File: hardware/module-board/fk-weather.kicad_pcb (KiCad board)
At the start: 2 copper layers, 37.5 x 103 mm, 72 parts, among them J1 MICRO-USB, J10 Conn_01x06, J11 Conn_01x06, J2 Conn_01x05, J3 CONN_01x03_SERIAL, J4 Conn_01x04, J5 Conn_01x02, J6 CONN_02x05_SWD, J7 Conn_01x05, Q4 2N7002LT1G, SW1 SPNO, U1 ATSAMD21G18A-AU, U2 MCP1700T-XXX2E, U3 TPS2051B, U4 S25FL1xxK0XM, U5 SK6812, U6 PCF8523, Y1 FC-135, Y2 FC-135

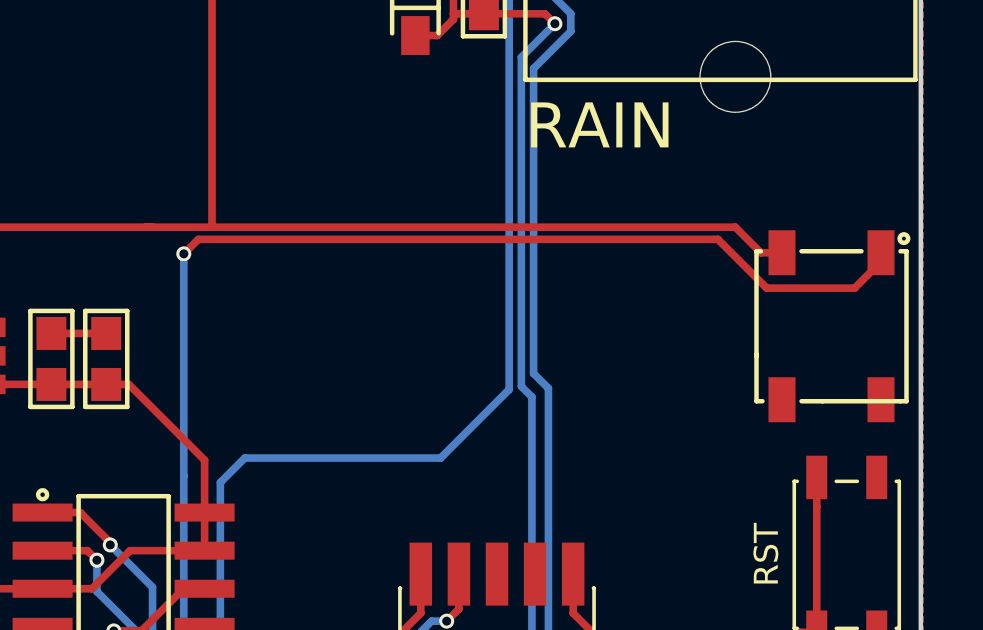
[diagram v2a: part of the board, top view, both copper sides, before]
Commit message: Fix SK6812 and cleanup signal naming.
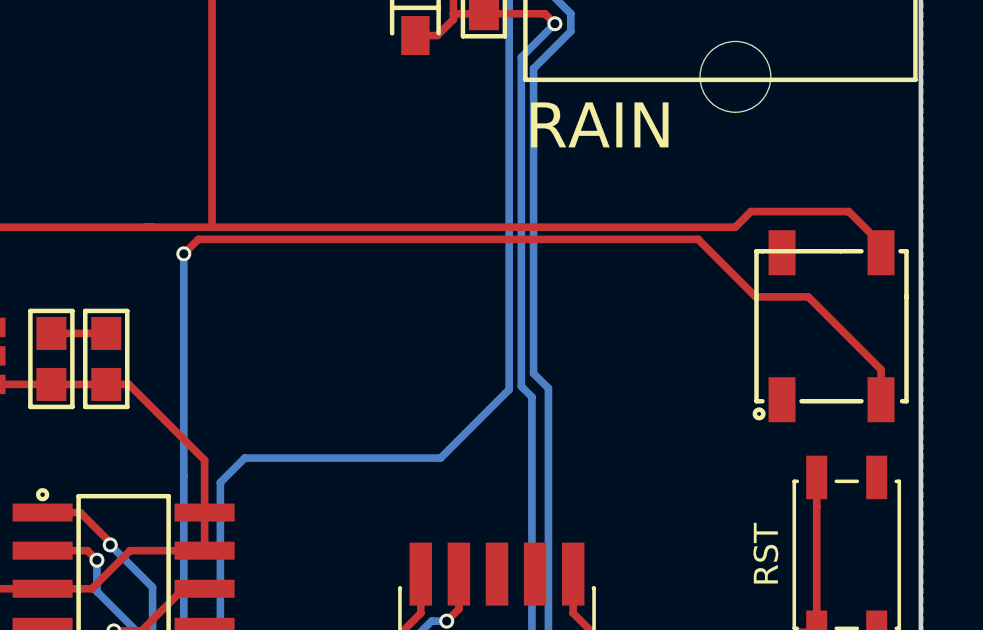
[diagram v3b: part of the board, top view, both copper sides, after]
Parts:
- C14: value 4.7uF 10V X5R -> 4.7uF
- C5: value 1uF 10V X5R -> 1uF
- J4: value Conn_01x04 -> CONN_01x04
- R8: value 100k -> 100K
- U2: value MCP1700T-XXX2E -> MCP1700T-3302E/MB
- U4: value S25FL1xxK0XM -> S25FL116K0XMFI041
- turned U5 to 270 degrees
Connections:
- net /FLASH_CS renamed /D5_FLASH_CS
- net /PERIPH_EN renamed /D8_PERIPH_EN
- net /RAIN renamed /D6_RAIN
- net /WIND_DIR renamed /A1_WIND_DIR
- net /WIND_SPEED renamed /D10_WIND_SPEED
- U5 pad 1: /A3 -> GND
- U5 pad 2: 3V3 -> /A3
- U5 pad 3: Net-(U5-Pad3) -> 3V3
- U5 pad 4: GND -> Net-(U5-Pad4)
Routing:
- net 3V3: track 285.5 -> 289.4 mm
- net /A3: track 52.1 -> 53.2 mm

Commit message: Fix rescued stuff and clear DRC problems.
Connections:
- net AREF renamed Net-(C14-Pad1)

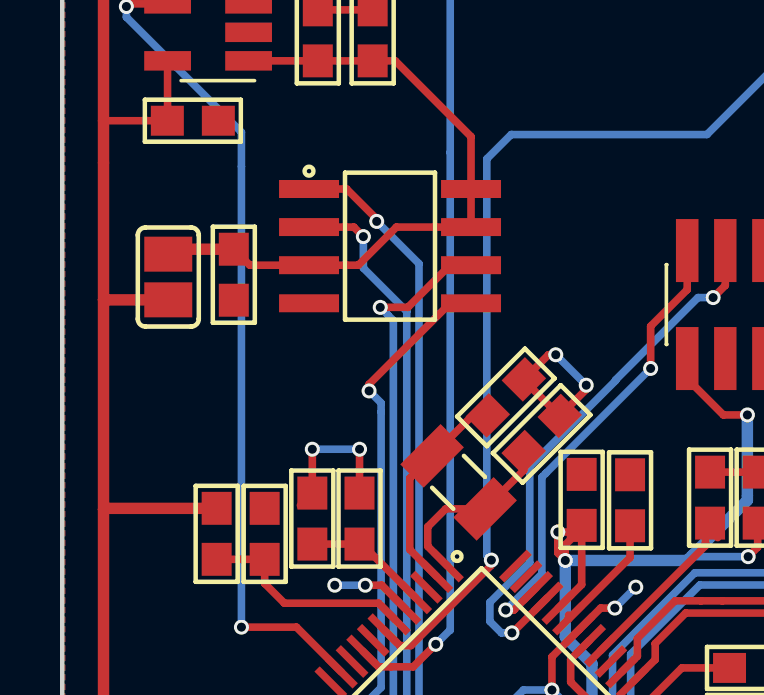
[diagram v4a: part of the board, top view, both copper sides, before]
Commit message: Use more compatible FP for flash.
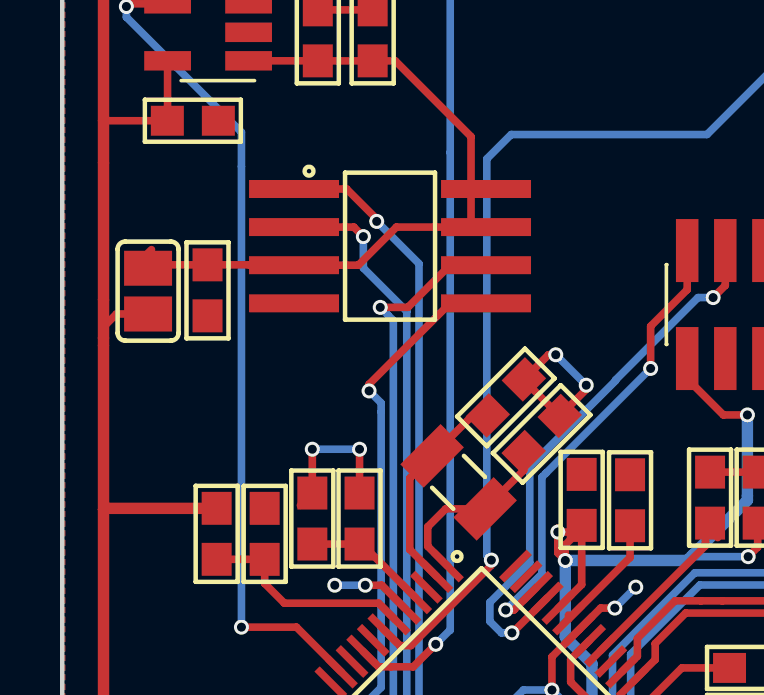
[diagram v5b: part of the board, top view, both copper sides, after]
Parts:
- U4: footprint conservify:SOIC-8-N -> conservify:SOIC-8-N-WIDE
- moved C18 1.02 mm to (89.4, 149.0)
- moved J5 0.82 mm to (87.5, 149.1)
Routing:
- net /PERIPH_3V3: track 22.4 -> 24.3 mm
- net 3V3: track 289.4 -> 290.4 mm

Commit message: Schematic/FP cleanup. Nothing major.
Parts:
- J10, J11: value Conn_01x06 -> CONN_01x06; footprint conservify:wurth_615006138421 -> conservify:WURTH_615006138421
- J2, J7: value Conn_01x05 -> CONN_01x05
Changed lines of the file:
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@@
       (xy -6.476371 -1.79874)) (layer F.SilkS) (width 0.01))
-  )
-  (module conservify:wurth_615006138421 (layer F.Cu)
-    (at 115.923028 125.132668 270)
-    (fp_text reference J10 (at 0 -3.01244 270) (layer F.SilkS) hide
-      (effects (font (size 0.762 0.762) (thickness 0.15)))
-    )
-    (fp_text value Conn_01x06 (at 0 0 270) (layer F.SilkS) hide
-      (effects (font (size 0.508 0.508) (thickness 0.127)))
-    )
-    (fp_line (start -6.1 -6) (end -6.1 7) (layer F.SilkS) (width 0.15))
-    (fp_line (start -6.1 7) (end 6.1 7) (layer F.SilkS) (width 0.15))
-    (fp_line (start 6.1 7) (end 6.1 -6) (layer F.SilkS) (width 0.15))
-    (fp_line (start -6.1 -6) (end 6.1 -6) (layer F.SilkS) (width 0.15))
-    (pad "" np_thru_hole circle (at -6 0 270) (size 2.36 2.36) (drill 2.36) (layers *.Cu *.Mask F.SilkS))
-    (pad "" np_thru_hole circle (at 6 0 270) (size 2.36 2.36) (drill 2.36) (layers *.Cu *.Mask F.SilkS))
-    (pad 1 thru_hole circle (at -2.55 4.84 270) (size 1.4 1.4) (drill 0.9) (layers *.Cu *.Mask)
-      (net 46 "Net-(J10-Pad1)"))
-    (pad 2 thru_hole circle (at -1.53 2.3 270) (size 1.4 1.4) (drill 0.9) (layers *.Cu *.Mask)
-      (net 47 /RAIN_2))
-    (pad 3 thru_hole circle (at -0.51 4.84 270) (size 1.4 1.4) (drill 0.9) (layers *.Cu *.Mask)
-      (net 48 "Net-(J10-Pad3)"))
-    (pad 4 thru_hole circle (at 0.51 2.3 270) (size 1.4 1.4) (drill 0.9) (layers *.Cu *.Mask)
-      (net 49 "Net-(J10-Pad4)"))
-    (pad 5 thru_hole circle (at 1.53 4.84 270) (size 1.4 1.4) (drill 0.9) (layers *.Cu *.Mask)
-      (net 50 /RAIN_5))
-    (pad 6 thru_hole circle (at 2.55 2.3 270) (size 1.4 1.4) (drill 0.9) (layers *.Cu *.Mask)
-      (net 51 "Net-(J10-Pad6)"))
-  )
-  (module conservify:wurth_615006138421 (layer F.Cu)
-    (at 115.937028 109.632668 270)
-    (fp_text reference J11 (at 0 -3.01244 270) (layer F.SilkS) hide
-      (effects (font (size 0.762 0.762) (thickness 0.15)))
-    )
-    (fp_text value Conn_01x06 (at 0 0 270) (layer F.SilkS) hide
-      (effects (font (size 0.508 0.508) (thickness 0.127)))
-    )
-    (fp_line (start -6.1 -6) (end -6.1 7) (layer F.SilkS) (width 0.15))
-    (fp_line (start -6.1 7) (end 6.1 7) (layer F.SilkS) (width 0.15))
-    (fp_line (start 6.1 7) (end 6.1 -6) (layer F.SilkS) (width 0.15))
-    (fp_line (start -6.1 -6) (end 6.1 -6) (layer F.SilkS) (width 0.15))
-    (pad "" np_thru_hole circle (at -6 0 270) (size 2.36 2.36) (drill 2.36) (layers *.Cu *.Mask F.SilkS))
-    (pad "" np_thru_hole circle (at 6 0 270) (size 2.36 2.36) (drill 2.36) (layers *.Cu *.Mask F.SilkS))
-    (pad 1 thru_hole circle (at -2.55 4.84 270) (size 1.4 1.4) (drill 0.9) (layers *.Cu *.Mask)
-      (net 52 "Net-(J11-Pad1)"))
-    (pad 2 thru_hole circle (at -1.53 2.3 270) (size 1.4 1.4) (drill 0.9) (layers *.Cu *.Mask)
-      (net 53 "Net-(J11-Pad2)"))
-    (pad 3 thru_hole circle (at -0.51 4.84 270) (size 1.4 1.4) (drill 0.9) (layers *.Cu *.Mask)
-      (net 54 "Net-(J11-Pad3)"))
-    (pad 4 thru_hole circle (at 0.51 2.3 270) (size 1.4 1.4) (drill 0.9) (layers *.Cu *.Mask)
-      (net 55 "Net-(J11-Pad4)"))
-    (pad 5 thru_hole circle (at 1.53 4.84 270) (size 1.4 1.4) (drill 0.9) (layers *.Cu *.Mask)
-      (net 56 "Net-(J11-Pad5)"))
-    (pad 6 thru_hole circle (at 2.55 2.3 270) (size 1.4 1.4) (drill 0.9) (layers *.Cu *.Mask)
-      (net 57 "Net-(J11-Pad6)"))
   )
   (module conservify:Molex_CLIK-Mate_502382-0570_1x05_P1.25mm_Vertical (layer F.Cu)
@@
       (effects (font (size 1 1) (thickness 0.15)))
     )
-    (fp_text value Conn_01x05 (at 0 4 270) (layer F.Fab) hide
+    (fp_text value CONN_01x05 (at 0 4 270) (layer F.Fab) hide
       (effects (font (size 1 1) (thickness 0.15)))
     )
@@
       (effects (font (size 1 1) (thickness 0.15)))
     )
-    (fp_text value Conn_01x05 (at 0 4 270) (layer F.Fab)
+    (fp_text value CONN_01x05 (at 0 4 270) (layer F.Fab)
       (effects (font (size 1 1) (thickness 0.15)))
     )
@@
     )
   )
+  (module conservify:WURTH_615006138421 (layer F.Cu)
+    (at 115.923028 125.132668 270)
+    (fp_text reference J10 (at 0 -3.01244 270) (layer F.SilkS) hide
+      (effects (font (size 0.762 0.762) (thickness 0.15)))
+    )
+    (fp_text value CONN_01x06 (at 0 0 270) (layer F.SilkS) hide
+      (effects (font (size 0.508 0.508) (thickness 0.127)))
+    )
+    (fp_line (start -6.1 -6) (end -6.1 7) (layer F.SilkS) (width 0.15))
+    (fp_line (start -6.1 7) (end 6.1 7) (layer F.SilkS) (width 0.15))
+    (fp_line (start 6.1 7) (end 6.1 -6) (layer F.SilkS) (width 0.15))
+    (fp_line (start -6.1 -6) (end 6.1 -6) (layer F.SilkS) (width 0.15))
+    (pad "" np_thru_hole circle (at -6 0 270) (size 2.36 2.36) (drill 2.36) (layers *.Cu *.Mask F.SilkS))
+    (pad "" np_thru_hole circle (at 6 0 270) (size 2.36 2.36) (drill 2.36) (layers *.Cu *.Mask F.SilkS))
+    (pad 1 thru_hole circle (at -2.55 4.84 270) (size 1.4 1.4) (drill 0.9) (layers *.Cu *.Mask)
+      (net 46 "Net-(J10-Pad1)"))
+    (pad 2 thru_hole circle (at -1.53 2.3 270) (size 1.4 1.4) (drill 0.9) (layers *.Cu *.Mask)
+      (net 47 /RAIN_2))
+    (pad 3 thru_hole circle (at -0.51 4.84 270) (size 1.4 1.4) (drill 0.9) (layers *.Cu *.Mask)
+      (net 48 "Net-(J10-Pad3)"))
+    (pad 4 thru_hole circle (at 0.51 2.3 270) (size 1.4 1.4) (drill 0.9) (layers *.Cu *.Mask)
+      (net 49 "Net-(J10-Pad4)"))
+    (pad 5 thru_hole circle (at 1.53 4.84 270) (size 1.4 1.4) (drill 0.9) (layers *.Cu *.Mask)
+      (net 50 /RAIN_5))
+    (pad 6 thru_hole circle (at 2.55 2.3 270) (size 1.4 1.4) (drill 0.9) (layers *.Cu *.Mask)
+      (net 51 "Net-(J10-Pad6)"))
+  )
+  (module conservify:WURTH_615006138421 (layer F.Cu)
+    (at 115.937028 109.632668 270)
+    (fp_text reference J11 (at 0 -3.01244 270) (layer F.SilkS) hide
+      (effects (font (size 0.762 0.762) (thickness 0.15)))
+    )
+    (fp_text value CONN_01x06 (at 0 0 270) (layer F.SilkS) hide
+      (effects (font (size 0.508 0.508) (thickness 0.127)))
+    )
+    (fp_line (start -6.1 -6) (end 6.1 -6) (layer F.SilkS) (width 0.15))
+    (fp_line (start 6.1 7) (end 6.1 -6) (layer F.SilkS) (width 0.15))
+    (fp_line (start -6.1 7) (end 6.1 7) (layer F.SilkS) (width 0.15))
+    (fp_line (start -6.1 -6) (end -6.1 7) (layer F.SilkS) (width 0.15))
+    (pad 6 thru_hole circle (at 2.55 2.3 270) (size 1.4 1.4) (drill 0.9) (layers *.Cu *.Mask)
+      (net 57 "Net-(J11-Pad6)"))
+    (pad 5 thru_hole circle (at 1.53 4.84 270) (size 1.4 1.4) (drill 0.9) (layers *.Cu *.Mask)
+      (net 56 "Net-(J11-Pad5)"))
+    (pad 4 thru_hole circle (at 0.51 2.3 270) (size 1.4 1.4) (drill 0.9) (layers *.Cu *.Mask)
+      (net 55 "Net-(J11-Pad4)"))
+    (pad 3 thru_hole circle (at -0.51 4.84 270) (size 1.4 1.4) (drill 0.9) (layers *.Cu *.Mask)
+      (net 54 "Net-(J11-Pad3)"))
+    (pad 2 thru_hole circle (at -1.53 2.3 270) (size 1.4 1.4) (drill 0.9) (layers *.Cu *.Mask)
+      (net 53 "Net-(J11-Pad2)"))
+    (pad 1 thru_hole circle (at -2.55 4.84 270) (size 1.4 1.4) (drill 0.9) (layers *.Cu *.Mask)
+      (net 52 "Net-(J11-Pad1)"))
+    (pad "" np_thru_hole circle (at 6 0 270) (size 2.36 2.36) (drill 2.36) (layers *.Cu *.Mask F.SilkS))
+    (pad "" np_thru_hole circle (at -6 0 270) (size 2.36 2.36) (drill 2.36) (layers *.Cu *.Mask F.SilkS))
+  )
   (gr_text SERIAL (at 113.792 159.131 90) (layer F.SilkS)

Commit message: Bump version and plot gerbers.
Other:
- board text added: "v0.10"
- board text removed: "v0.9"
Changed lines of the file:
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@@
     (effects (font (size 0.6 0.6) (thickness 0.11)))
   )
-  (gr_text v0.9 (at 110.998 199.136) (layer F.SilkS)
+  (gr_text v0.10 (at 110.8583 199.0471) (layer F.SilkS)
     (effects (font (size 1.2 1.2) (thickness 0.2)))
   )
